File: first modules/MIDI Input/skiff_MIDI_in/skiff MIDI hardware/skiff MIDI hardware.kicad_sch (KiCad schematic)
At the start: 14 parts, among them J2 AudioJack3, J3 DIN-5, U1 H11L1

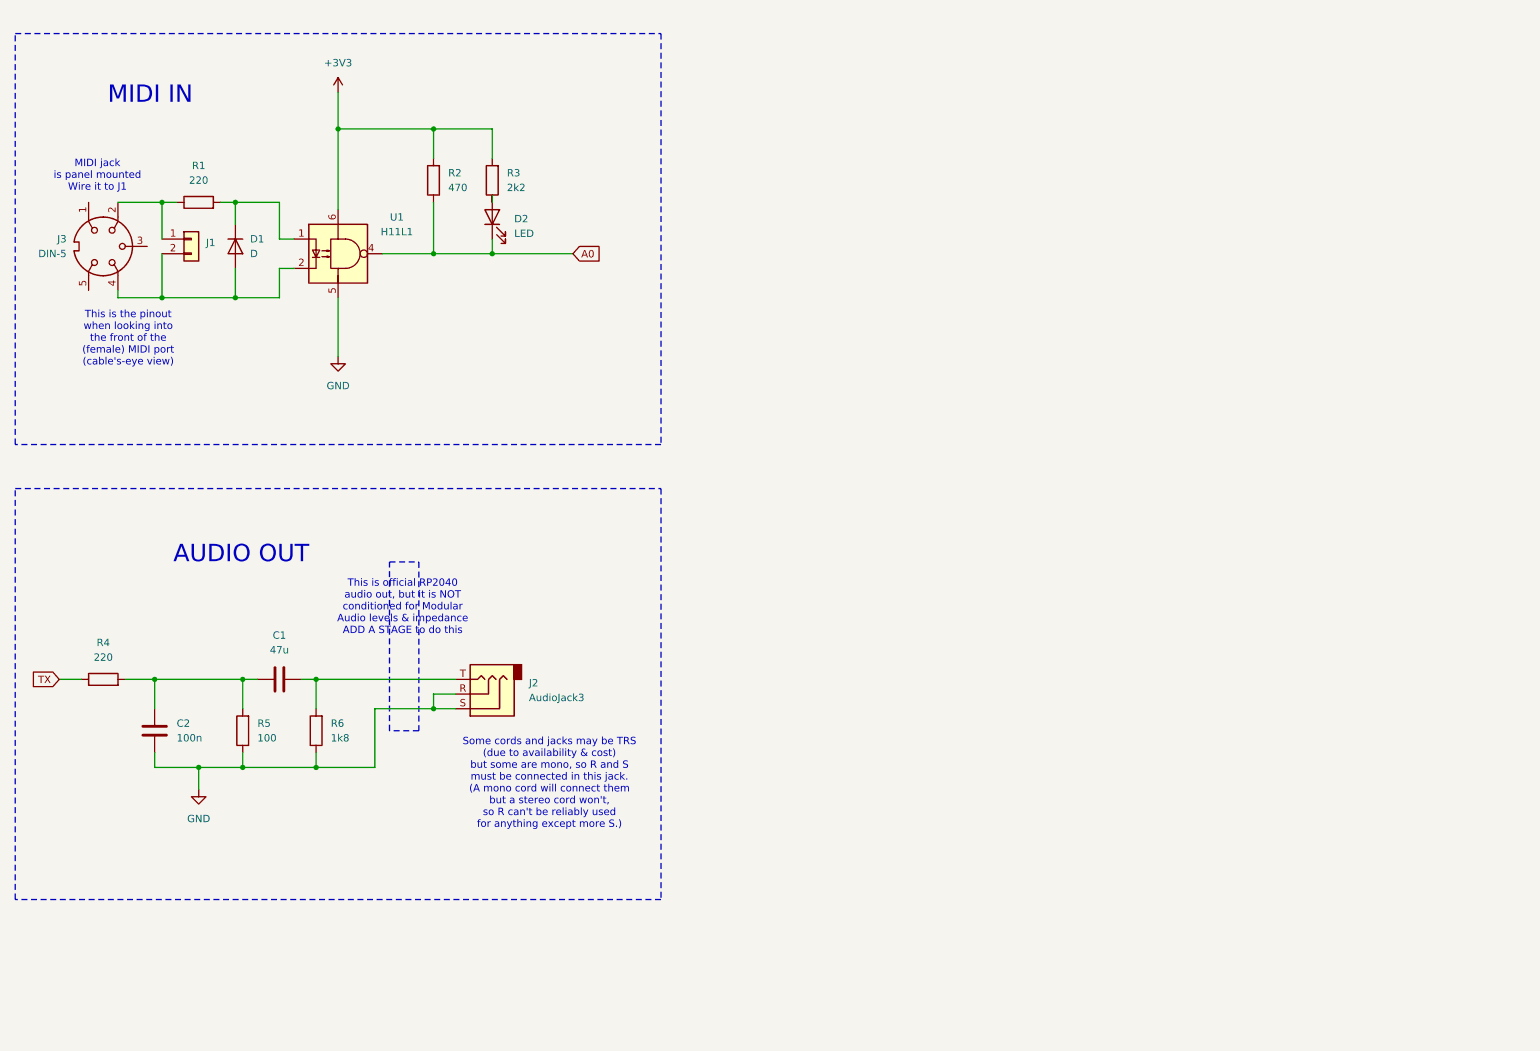
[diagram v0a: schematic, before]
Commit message: PCB in progress; Schematic lacks only output stages (Outputs don't yet conform to Modular Synth signal standards, but schematic should be otherwise ok.)
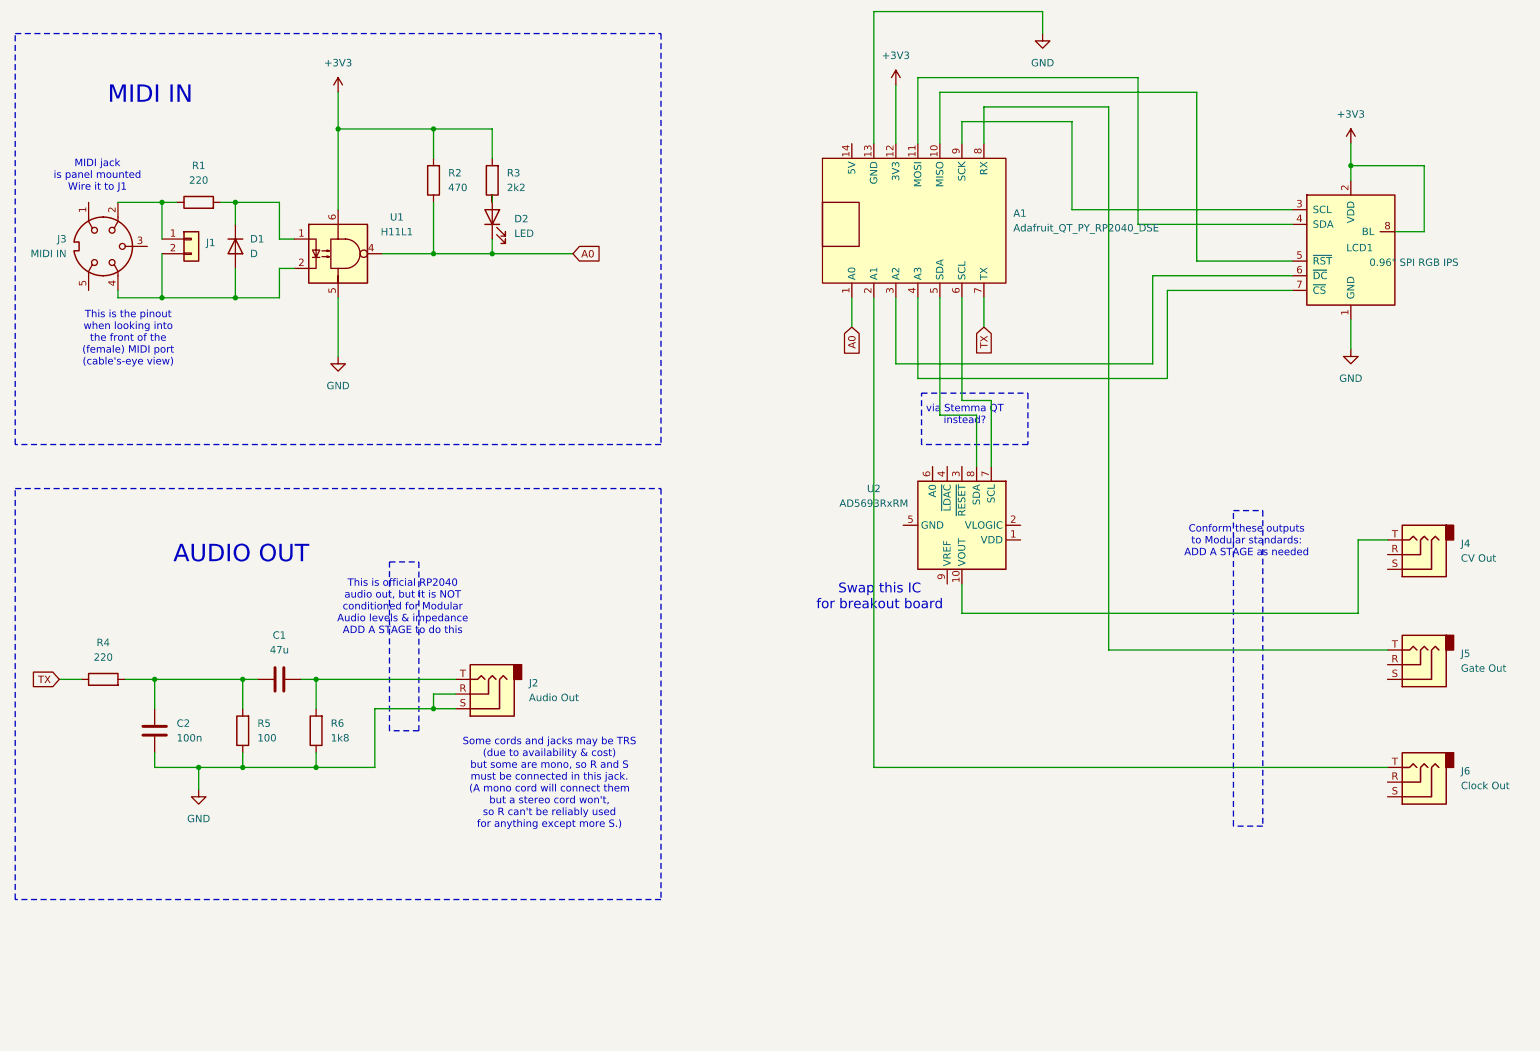
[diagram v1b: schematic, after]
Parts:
- added A1: Adafruit_QT_PY_RP2040_DSE, DSE_Custom_Footprints:Adafruit_QT_PY_RP2040_DSE, symbol DSE Custom KiCad Parts Library:Adafruit_QT_PY_RP2040_DSE
- added J4: CV Out, Connector_Audio:Jack_3.5mm_QingPu_WQP-PJ398SM_Vertical_CircularHoles, symbol Connector_Audio:AudioJack3
- added J5: Gate Out, Connector_Audio:Jack_3.5mm_QingPu_WQP-PJ398SM_Vertical_CircularHoles, symbol Connector_Audio:AudioJack3
- added J6: Clock Out, Connector_Audio:Jack_3.5mm_QingPu_WQP-PJ398SM_Vertical_CircularHoles, symbol Connector_Audio:AudioJack3
- added LCD1: 0.96" SPI RGB IPS, Controller: SSD1306, symbol DSE Custom KiCad Parts Library:ST7735S_RGB_IPS_80x160_Breakout_DSE
- added U2: AD5693RxRM, Package_SO:MSOP-10_3x3mm_P0.5mm, symbol Analog_DAC:AD5693RxRM
- J2: value AudioJack3 -> Audio Out
- J3: value DIN-5 -> MIDI IN
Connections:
- net +3V3: now also A1.12 (3V3), LCD1.2 (VDD), LCD1.8 (BL)
- net A0: now also A1.1 (A0)
- net GND: now also A1.13 (GND), LCD1.1 (GND)
- net TX: now also A1.7 (TX)
- new net: J4.T, U2.10 (VOUT)
- new net: A1.6 (SCL), U2.7 (SCL)
- new net: A1.5 (SDA), U2.8 (SDA)
- new net: A1.2 (A1), J6.T
- new net: A1.8 (RX), J5.T
- new net: A1.10 (MISO), LCD1.5 (~{RST})
- new net: A1.11 (MOSI), LCD1.4 (SDA)
- new net: A1.3 (A2), LCD1.6 (~{DC})
- new net: A1.4 (A3), LCD1.7 (~{CS})
- new net: A1.9 (SCK), LCD1.3 (SCL)
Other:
- note added: "Conform these outputs to Modular standards: ADD A STAGE as needed"
- note added: "Swap this IC for breakout board"
- note added: "via Stemma QT instead?"

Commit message: Sch: Add Rotary Encoder; move DAC to Stemma QT i2c; Remove Clock output (it was an optional bonus, but there's no pin available for it. I suppose we could chain additional outputs onto the Stemma QT bus... that can be left as an option for future expansion)
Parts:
- removed J6: Clock Out, Connector_Audio:Jack_3.5mm_QingPu_WQP-PJ398SM_Vertical_CircularHoles, symbol Connector_Audio:AudioJack3
- added SW1: RotaryEncoder_Switch, symbol Device:RotaryEncoder_Switch
- A1: value Adafruit_QT_PY_RP2040_DSE -> Adafruit_QT_PY; footprint DSE_Custom_Footprints:Adafruit_QT_PY_RP2040_DSE -> DSE Custom KiCad Parts Library:Adafruit QT PY RP2040
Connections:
- net GND: now also SW1.C, SW1.S1
- net at A1.6 (SCL): now also SW1.A; no longer U2.7 (SCL)
- net at A1.5 (SDA): now also SW1.B; no longer U2.8 (SDA)
- net at A1.2 (A1): now also SW1.S2
- new net SCL1: A1.23 (SCL1), U2.7 (SCL)
- new net SDA1: A1.22 (SDA1), U2.8 (SDA)
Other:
- note removed: "via Stemma QT instead?"
- moved on the sheet: U2

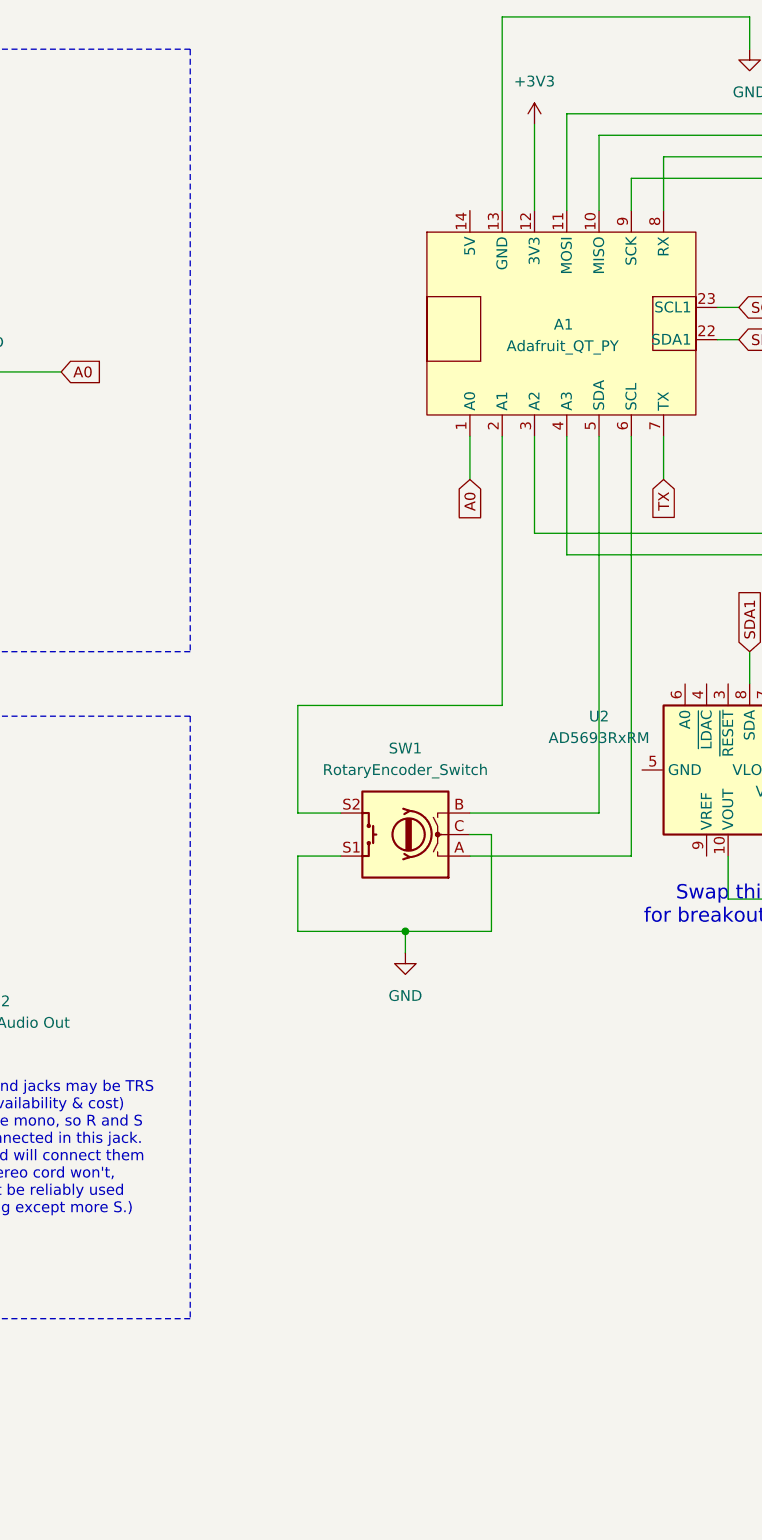
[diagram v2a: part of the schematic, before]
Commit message: Schematic: add power switch. minor cleanup.
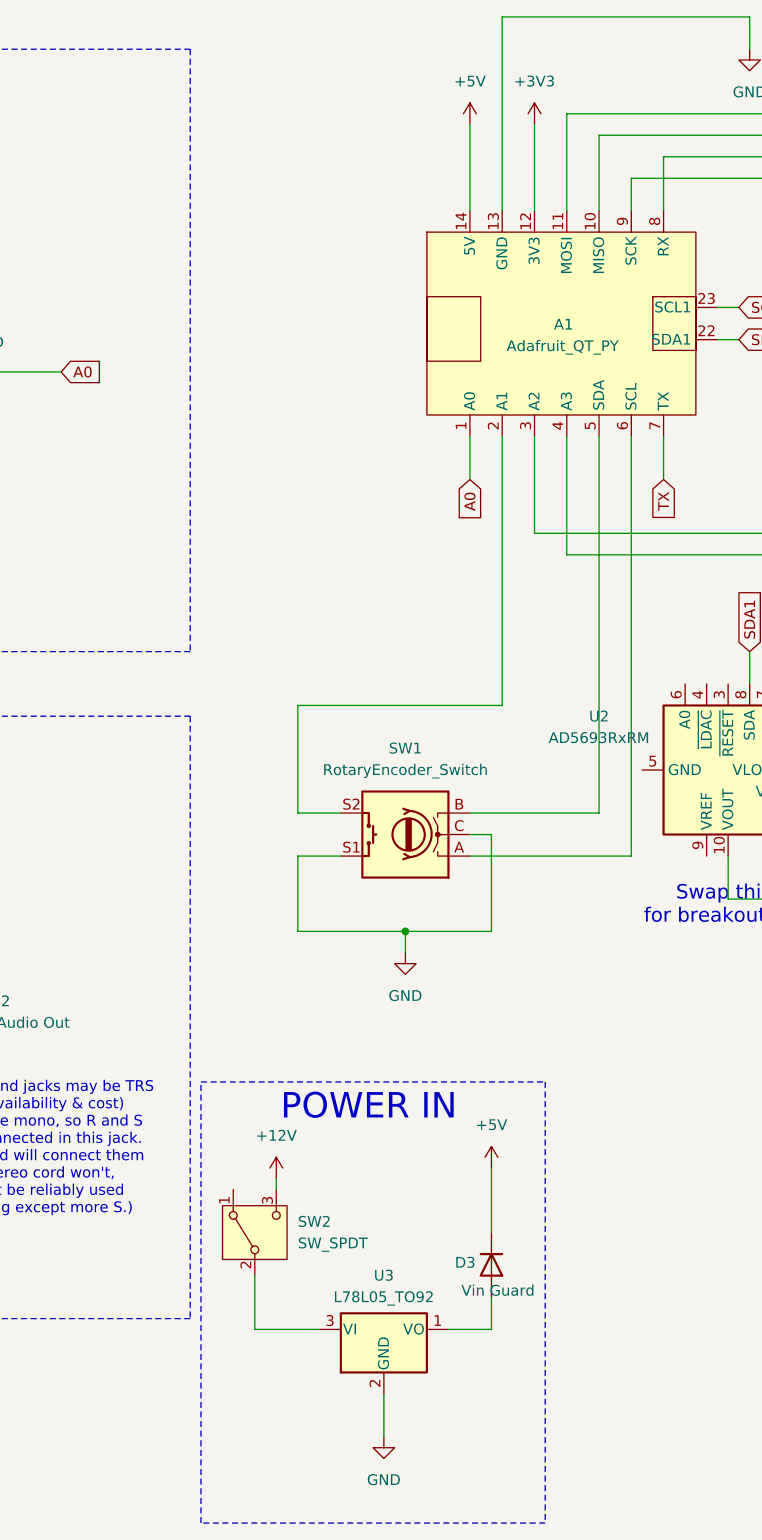
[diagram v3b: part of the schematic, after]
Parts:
- added D3: Vin Guard, symbol Device:D
- added SW2: SW_SPDT, symbol Switch:SW_SPDT
- added U3: L78L05_TO92, Package_TO_SOT_THT:TO-92_Inline, symbol Regulator_Linear:L78L05_TO92
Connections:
- net GND: now also U3.2 (GND)
- net +5V: now reaches A1.14 (5V)
- net +5V: now also D3.1 (K)
- new net: SW2.2 (B), U3.3 (VI)
- new net: D3.2 (A), U3.1 (VO)
- new net +12V: SW2.3 (C)
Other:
- note added: "POWER IN"
